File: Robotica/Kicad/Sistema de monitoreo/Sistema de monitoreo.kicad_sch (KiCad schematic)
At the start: 0 parts

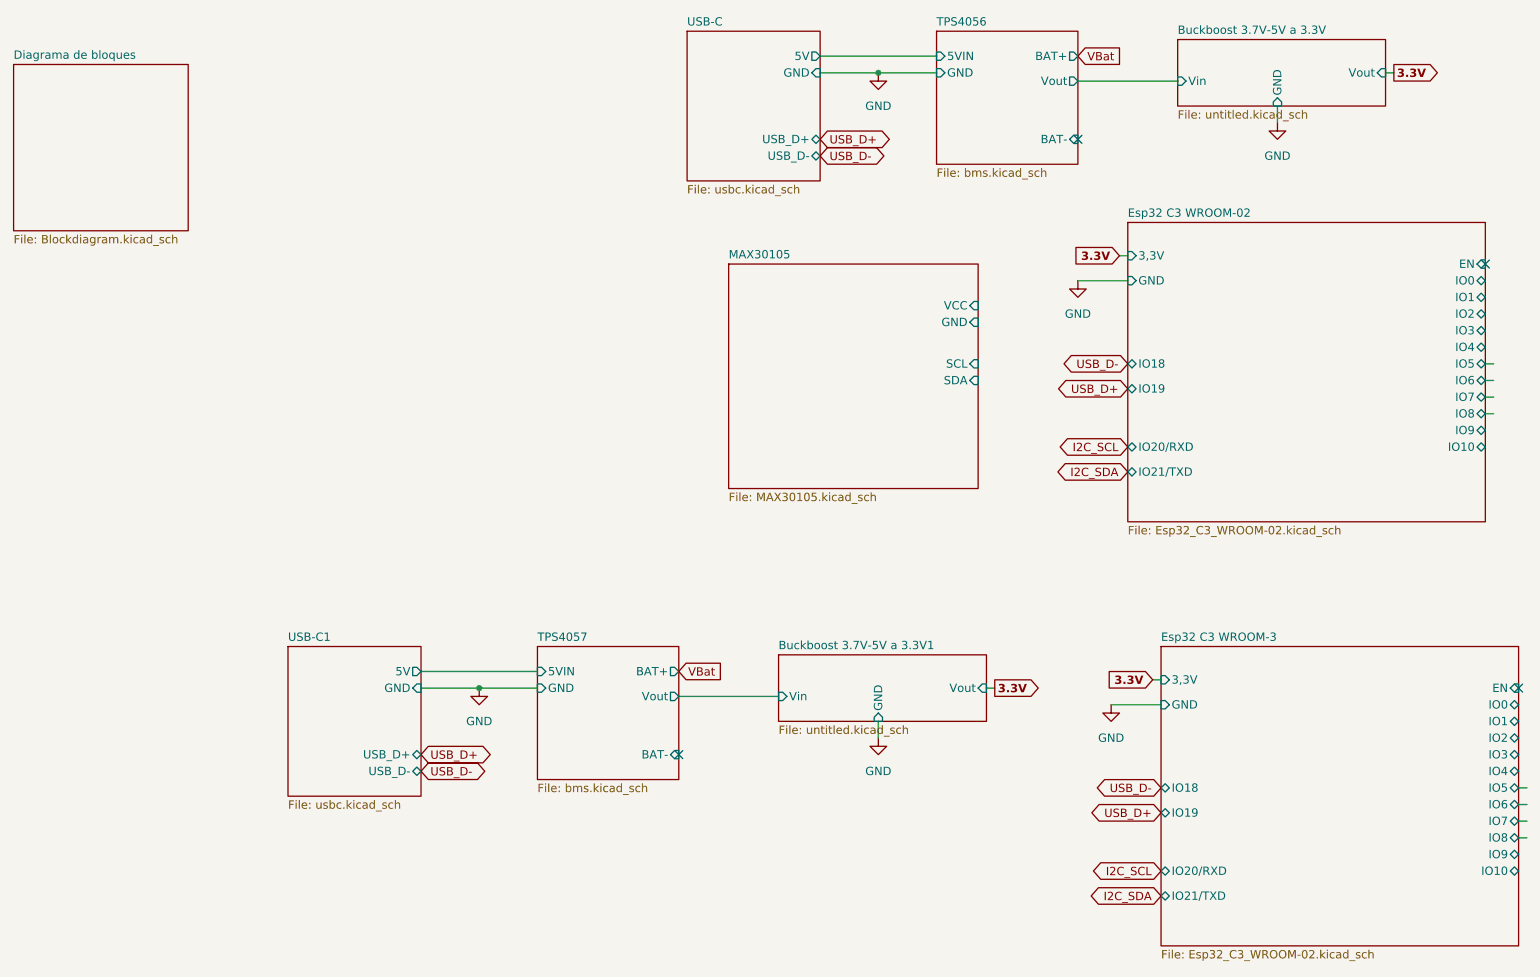
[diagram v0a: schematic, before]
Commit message: Organizacion de esquematicos de robotica
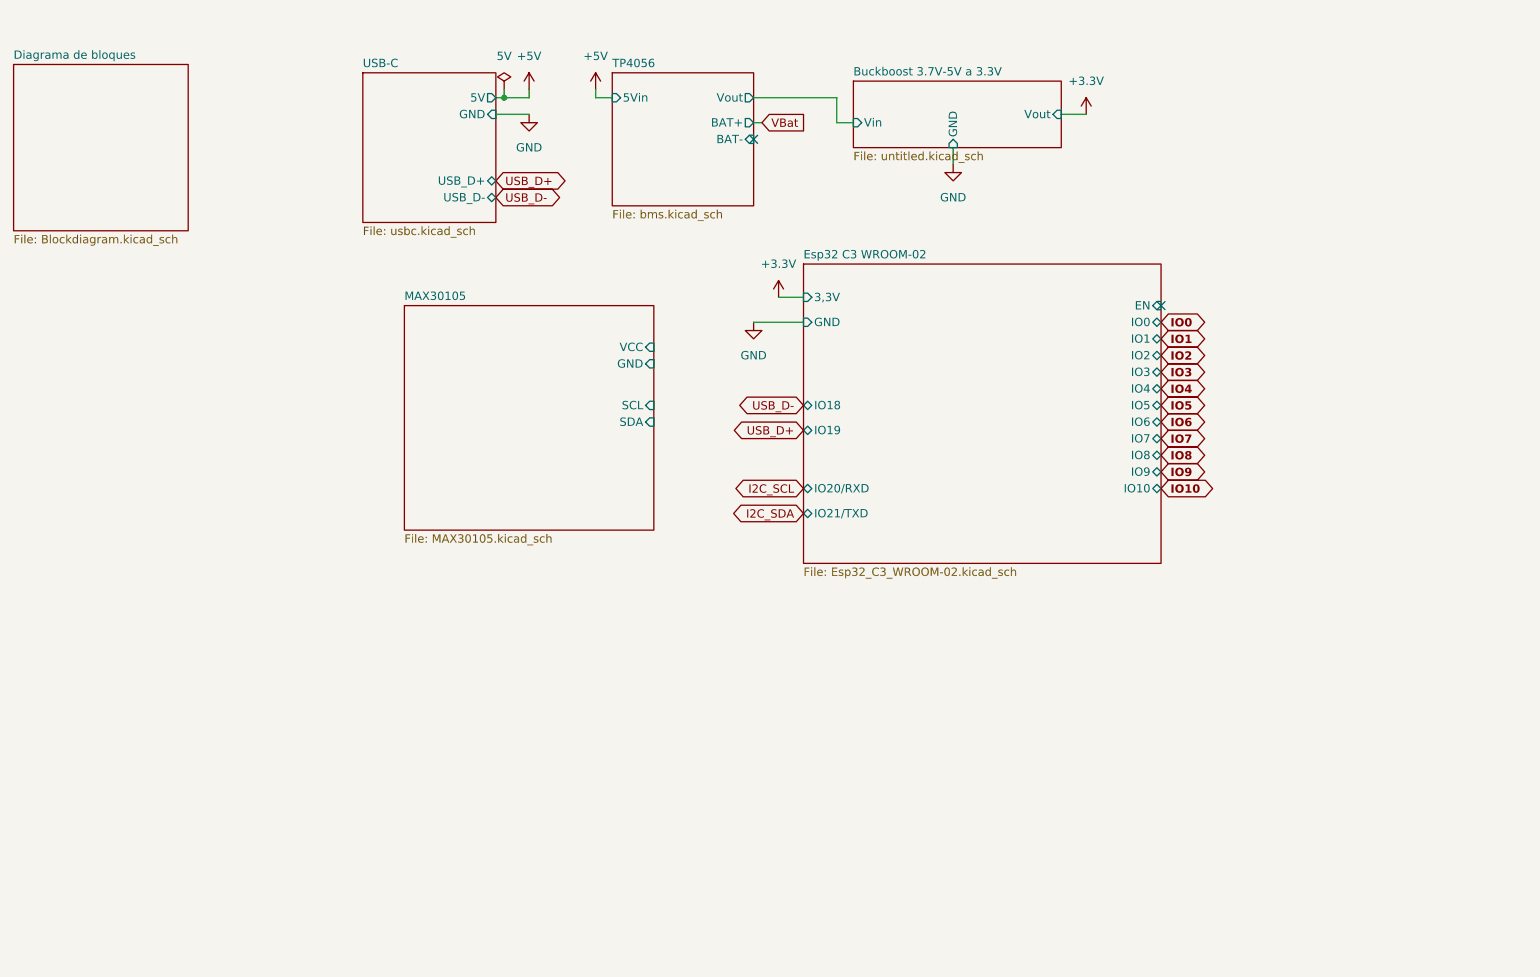
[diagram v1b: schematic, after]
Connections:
- no-connect marks 4 -> 2
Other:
- sheet TPS4056 renamed TP4056
- removed sheet Buckboost 3.7V-5V a 3.3V1
- removed sheet Esp32 C3 WROOM-3
- removed sheet TPS4057
- removed sheet USB-C1
- sheet TP4056 ports: added 5Vin; removed 5VIN, GND
